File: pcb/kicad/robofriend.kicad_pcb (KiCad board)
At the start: 2 copper layers, 124 parts, among them J1 I2C, J10 BAT2, J11 5VIN, J12 BAT3, J13 3V3OUT, J14 3V3OUT, J15 SPI, J16 MON, J17 M1, J18 M2, J19 US4, J2 ADC1, J20 5VOUT, J21 5VOUT, J22 US3, J23 US2, J24 US1, J25 I2C, J26 I2C, J27 I2C, J28 ADC4, J29 AMP, J3 ADC2, J30 PWR, J31 MLe, J32 USB_A_4_PIN, J4 UART, J5 ADC3, J6 ADC4, J7 BAT1, J8 MRi, J9 12VOUT, K2 SCHRACK-RTx3, Q1 NMOS, Q2 NMOS, Q3 NPN, Q4 PMOS, Q5 NMOS, Q6 NMOS, Q7 NMOS, Q8 NMOS, U1 Teensy++2.0, U2 LM4040, U3 LM321, U4 LM321, U5 LM3940-3.3

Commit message: first steps of layouting done
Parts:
- removed the C14 at (55.9, 120.7)
- removed the C20 at (68.6, 106.0)
- removed the D12 at (64.8, 129.5)
- removed the J29 at (-3.81, 119.4)
- removed K2: SCHRACK-RTx3, SLA_12VDC:Relay_SPST_Schrack-RTx3_RM3.5mm
- removed the Q2 at (88.9, 162.6)
- removed the R19 at (91.1, 143.2)
- removed the R20 at (91.1, 146.4)
- removed the R9 at (92.7, 172.1)
- removed the U4 at (84.1, 147.0)
- added C17: 1n, Capacitors_SMD:C_0805, F.Cu at (206.4, 130.2)
- added C18: 10n, Capacitors_SMD:C_0805, F.Cu at (206.4, 134.0)
- added C21: 100n, Capacitors_SMD:C_0805, F.Cu at (215.3, 137.2)
- added C24: 100n, Capacitors_SMD:C_0805, F.Cu at (219.7, 130.8)
- added C4: 33u, Capacitors_SMD:CP_Elec_4x5.7, F.Cu at (175.3, 59.1)
- added C5: 100u, Capacitors_SMD:CP_Elec_6.3x5.7, F.Cu at (117.5, 65.4)
- added C6: 33u, Capacitors_SMD:CP_Elec_5x5.7, F.Cu at (127.6, 87.0)
- added D15: BAT54, Diodes_SMD:D_SOD-323, F.Cu at (143.8, 124.1)
- added D16: BAT54, Diodes_SMD:D_SOD-323, F.Cu at (143.8, 121.0)
- added D2: D, Diodes_SMD:D_SOD-323, F.Cu at (115.6, 88.9)
- added D20: BAT54, Diodes_SMD:D_SOD-123, F.Cu at (208.3, 141.6)
- added J33: GS2, Connectors:GS2, F.Cu at (219.7, 138.4)
- added J8: GS2, Connectors:GS2, F.Cu at (121.9, 85.7)
- added JP3: JP, Pin_Headers:Pin_Header_Straight_1x02_Pitch2.54mm, F.Cu at (152.1, 121.0)
- added K1: SCHRACK-RTx3, Relay:SPST_Schrack-RTx3_RM3.5mm, F.Cu at (114.3, 69.8)
- added R1: 4.7k, Resistors_SMD:R_0805, F.Cu at (141.0, 91.4)
- added R13: 12k, Resistors_SMD:R_0805, F.Cu at (141.9, 124.1)
- added R18: 39k, Resistors_SMD:R_0805, F.Cu at (140.0, 121.0)
- added R2: 47k, Resistors_SMD:R_0805, F.Cu at (135.9, 91.4)
- added R3: 20k, Resistors_SMD:R_0805, F.Cu at (117.5, 92.1)
- added R4: 10k, Resistors_SMD:R_0805, F.Cu at (120.7, 92.1)
- added R5: 1M, Resistors_SMD:R_0805, F.Cu at (121.9, 88.9)
- added U5: MCP6001, TO_SOT_Packages_SMD:SOT-23-5, F.Cu at (147.0, 122.2)
- added U6: INA193, TO_SOT_Packages_SMD:SOT-23-5, F.Cu at (215.3, 134.0)
- added U7: TL331, TO_SOT_Packages_SMD:SOT-23-5, F.Cu at (219.7, 134.0)
- C10: renamed from C18; moved to B.Cu
- C11: value 15n -> 47u; footprint Capacitors_SMD:C_0805 -> Capacitors_SMD:CP_Elec_6.3x5.8
- C12: value 100n -> 470u; footprint Capacitors_SMD:C_0805 -> Capacitors_SMD:CP_Elec_8x10.5
- C13: renamed from C21; moved to B.Cu
- C14: renamed from C22; moved to B.Cu
- C15: renamed from C3; moved to B.Cu
- C16: renamed from C4; moved to B.Cu
- C19: value 47u -> 1n; footprint Capacitors_SMD:CP_Elec_6.3x5.3 -> Capacitors_SMD:C_0805
- C20: renamed from C5; moved to B.Cu
- C22: renamed from C6; moved to B.Cu
- C26: renamed from C7; moved to B.Cu
- C27: renamed from C8; moved to B.Cu
- C7: renamed from C15; moved to B.Cu
- C8: renamed from C16; moved to B.Cu
- C9: renamed from C17; moved to B.Cu
- D1: renamed from D10; value 10V -> 6V2
- D11: renamed from D8; moved to B.Cu
- D12: renamed from D9; moved to B.Cu
- D13: renamed from D20; moved to B.Cu
- D14: renamed from D21; moved to B.Cu
- D18: renamed from D2; moved to B.Cu
- D19: renamed from D3; moved to B.Cu
- D21: renamed from D6; moved to B.Cu
- D22: renamed from D7; moved to B.Cu
- D23: renamed from D4; moved to B.Cu
- D24: renamed from D5; moved to B.Cu
- J21: renamed from J16; value MON -> MON/AMP
- Q1: footprint TO_SOT_Packages_THT:TO-220-3_Vertical -> TO_SOT_Packages_SMD:SOT-23
- Q2: renamed from Q7; moved to B.Cu
- Q3: renamed from Q8; moved to B.Cu
- R10: renamed from R26; moved to B.Cu
- R11: renamed from R27; moved to B.Cu
- R12: renamed from R5; moved to B.Cu
- R14: renamed from R10; value 100k -> 18k
- R16: renamed from R11; value 27k -> 3k
- R19: renamed from R21; moved to B.Cu
- R23: renamed from R2; moved to B.Cu
- R24: renamed from R17; value 1k -> 100
- R25: renamed from R18; value 1k -> 100
- R26: renamed from R4; moved to B.Cu
- R29: renamed from R3; moved to B.Cu
- R7: renamed from R6; moved to B.Cu
- R8: renamed from R7; moved to B.Cu
- R9: renamed from R8; value 909 -> 910; moved to F.Cu
- U3: value LM321 -> TL331
- U4: renamed from U2; moved to F.Cu
- moved J20 220.2 mm to (201.9, 45.1), turned to 180 degrees
- moved R27 207.3 mm to (203.8, 114.9), turned to 90 degrees
- moved R11 206.0 mm to (191.1, 81.9), turned to 270 degrees
- moved Q6 205.4 mm to (194.9, 113.0), turned to 180 degrees
- moved R28 203.7 mm to (203.8, 117.5), turned to 270 degrees
- moved R30 201.8 mm to (194.9, 115.6)
- moved R10 200.6 mm to (191.1, 79.4), turned to 90 degrees
- moved Q7 199.3 mm to (194.9, 118.1), turned to 180 degrees
- moved Q2 198.6 mm to (188.0, 78.7), turned to 180 degrees
- moved R31 195.4 mm to (194.9, 120.7)
- moved C14 193.5 mm to (199.4, 71.8), turned to 180 degrees
- moved Q3 193.5 mm to (188.0, 82.5), turned to 180 degrees
- moved C13 191.6 mm to (195.6, 71.8), turned to 0 degrees
- moved C23 180.5 mm to (214.0, 115.6)
- moved C25 180.0 mm to (214.0, 119.4)
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- renumbered C13 to C1, C1 to C2, C9 to C23, C10 to C25, C2 to C3, D19 to D10, D13 to D17, D11 to D3, D1 to D4, D14 to D5, D15 to D6, D16 to D7, D17 to D8, D18 to D9, J7 to J1, J22 to J10, J19 to J11, J1 to J12, J25 to J13, J26 to J14, J27 to J15, J9 to J16, J11 to J17, J20 to J18, J21 to J19, J10 to J2, J32 to J20, J6 to J22, J8 to J23, J15 to J24, J28 to J25, J31 to J26, J17 to J27, J18 to J28, J2 to J29, J12 to J3, J3 to J30, J4 to J31, J5 to J32, J30 to J4, J24 to J5, J13 to J6, J14 to J7, J23 to J9, JP6 to JP2, JP3 to JP4, JP4 to JP5, JP2 to JP6, JP5 to JP7, Q3 to Q4, Q4 to Q5, Q5 to Q6, Q6 to Q7, R12 to R15, R13 to R17, R14 to R20, R15 to R21, R16 to R22, R22 to R27, R23 to R28, R24 to R30, R25 to R31, R1 to R6, U5 to U1, U1 to U2
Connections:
- C10 pad 2: +SW -> +12V
- C11 pad 1: Net-(C11-Pad1) -> +12V
- C11 pad 2: +SW -> GND
- C12 pad 1: GND -> +12V
- C12 pad 2: F0 -> GND
- C19 pad 1: +SW -> Net-(C18-Pad2)
- C7 pad 2: +SW -> +12V
- C8 pad 2: +SW -> +12V
- C9 pad 2: +SW -> +12V
- D1 pad 1: Net-(C11-Pad1) -> Net-(D1-Pad1)
- D1 pad 2: Net-(D1-Pad1) -> GND
- D10 pad 1: Net-(D19-Pad1) -> (no net)
- D10 pad 2: Net-(D19-Pad2) -> (no net)
- D3 pad 1: +SW -> -SW
- D3 pad 2: Net-(D11-Pad2) -> Net-(D3-Pad2)
- D4 pad 1: Net-(D1-Pad1) -> GND
- D5 pad 1: Net-(D14-Pad1) -> (no net)
- D5 pad 2: Net-(D14-Pad2) -> (no net)
- D6 pad 1: Net-(D15-Pad1) -> (no net)
- D6 pad 2: Net-(D15-Pad2) -> (no net)
- D7 pad 1: Net-(D16-Pad1) -> (no net)
- D7 pad 2: Net-(D16-Pad2) -> (no net)
- D8 pad 1: Net-(D17-Pad1) -> (no net)
- D8 pad 2: Net-(D17-Pad2) (its old number) -> (no net)
- D9 pad 1: Net-(D18-Pad1) (its old number) -> (no net)
- D9 pad 2: Net-(D18-Pad2) -> (no net)
- J1 pad 1: -SW -> +SW
- J16 pad 1: +SW -> +12V
- J2 pad 1: -SW -> +SW
- J20 pad 2: Net-(J32-Pad2) (its old number) -> (no net)
- J20 pad 3: Net-(J32-Pad3) -> (no net)
- J21 pad 1: Net-(J16-Pad1) -> +12V
- J21 pad 2: Net-(J16-Pad2) -> +12V
- J21 pad 3: Net-(J16-Pad3) -> +5V
- J21 pad 4: Net-(J16-Pad4) -> GND
- J21 pad 5: Net-(J16-Pad5) -> GND
- J21 pad 6: Net-(J16-Pad6) -> GND
- J23 pad 7: Net-(J8-Pad7) -> (no net)
- J23 pad 8: Net-(J8-Pad8) -> (no net)
- J23 pad 9: Net-(J8-Pad9) -> (no net)
- J26 pad 7: Net-(J31-Pad7) -> (no net)
- J26 pad 8: Net-(J31-Pad8) -> (no net)
- J26 pad 9: Net-(J31-Pad9) -> (no net)
- J3 pad 1: -SW -> +SW
- J4 pad 2: +12P -> +SW
- Q1 pad 1: GND -> Net-(D3-Pad2)
- Q1 pad 2: Net-(C11-Pad1) -> Net-(Q1-Pad2)
- Q1 pad 3: Net-(D1-Pad1) -> GND
- Q5 pad 3: +SW -> +12V
- R14 pad 1: F0 -> Net-(D15-Pad2)
- R14 pad 2: +SW -> +12V
- R16 pad 1: F0 -> Net-(D15-Pad2)
- R20 pad 1: +SW -> +12V
- R24 pad 1: Net-(R17-Pad1) -> Net-(C17-Pad2)
- R25 pad 1: Net-(R18-Pad1) -> Net-(C18-Pad2)
- R6 pad 1: +SW -> +12V
- R9 pad 2: AREF -> Net-(JP3-Pad2)
- RV1 pad 1: +SW -> Net-(D1-Pad1)
- RV1 pad 2: Net-(Q2-Pad2) -> Net-(RV1-Pad2)
- RV1 pad 3: Net-(D1-Pad1) -> Net-(R2-Pad1)
- U2 pad 24: /F7 -> (no net)
- U2 pad 25: /F6 -> F6
- U2 pad 43: Net-(U1-Pad43) -> (no net)
- U2 pad 44: Net-(U1-Pad44) -> (no net)
- U2 pad 45: Net-(U1-Pad45) -> (no net)
- U2 pad 46: Net-(U1-Pad46) -> (no net)
- U2 pad 47: Net-(U1-Pad47) -> (no net)
- U2 pad 48: Net-(U1-Pad48) -> (no net)
- U2 pad 49: Net-(U1-Pad49) -> (no net)
- U2 pad 50: Net-(U1-Pad50) -> (no net)
- U2 pad 51: Net-(U1-Pad51) -> (no net)
- U2 pad 52: Net-(U1-Pad52) -> (no net)
- U3 pad 1: Net-(R17-Pad1) -> Net-(RV1-Pad2)
- U3 pad 3: Net-(R18-Pad1) -> Net-(J8-Pad2)
- U3 pad 4: Net-(R20-Pad1) -> Net-(Q1-Pad2)
- U3 pad 5: +5V -> Net-(D2-Pad1)
- U4 pad 1: AREF -> Net-(JP3-Pad2)
- U4 pad 3: Net-(U2-Pad3) -> (no net)
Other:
- net class Power added: clearance 0.2, trace_width 1, via_dia 0.6, via_drill 0.4
- board text added: "1"
- board text added: "12V"
- board text added: "2"
- board text added: "3"
- board text added: "3V3"
- board text added: "4"
- board text added: "5V"
- board text added: "ADC1"
- board text added: "ADC2"
- board text added: "BAT1"
- board text added: "Boost"
- board text added: "Buck-In"
- board text added: "Buck-Out"
- board text added: "ECHO"
- board text added: "GND"
- board text added: "I2C"
- board text added: "IR1"
- board text added: "IR2"
- board text added: "IR3"
- board text added: "MISO"
- board text added: "MLe"
- board text added: "MOSI"
- board text added: "MRi"
- board text added: "Main-Switch"
- board text added: "Monitor/Amp"
- board text added: "RST"
- board text added: "RX"
- board text added: "RoboFriend - Power PCB Designed by Martin Zahedi University of Applied Sciences - Technikum Wien"
- board text added: "SCK"
- board text added: "SCL"
- board text added: "SDA"
- board text added: "SIG"
- board text added: "SPI"
- board text added: "SS"
- board text added: "TRIG"
- board text added: "TX"
- board text added: "UART"
- board text added: "Ultrasonic"
- board text added: "VCC"

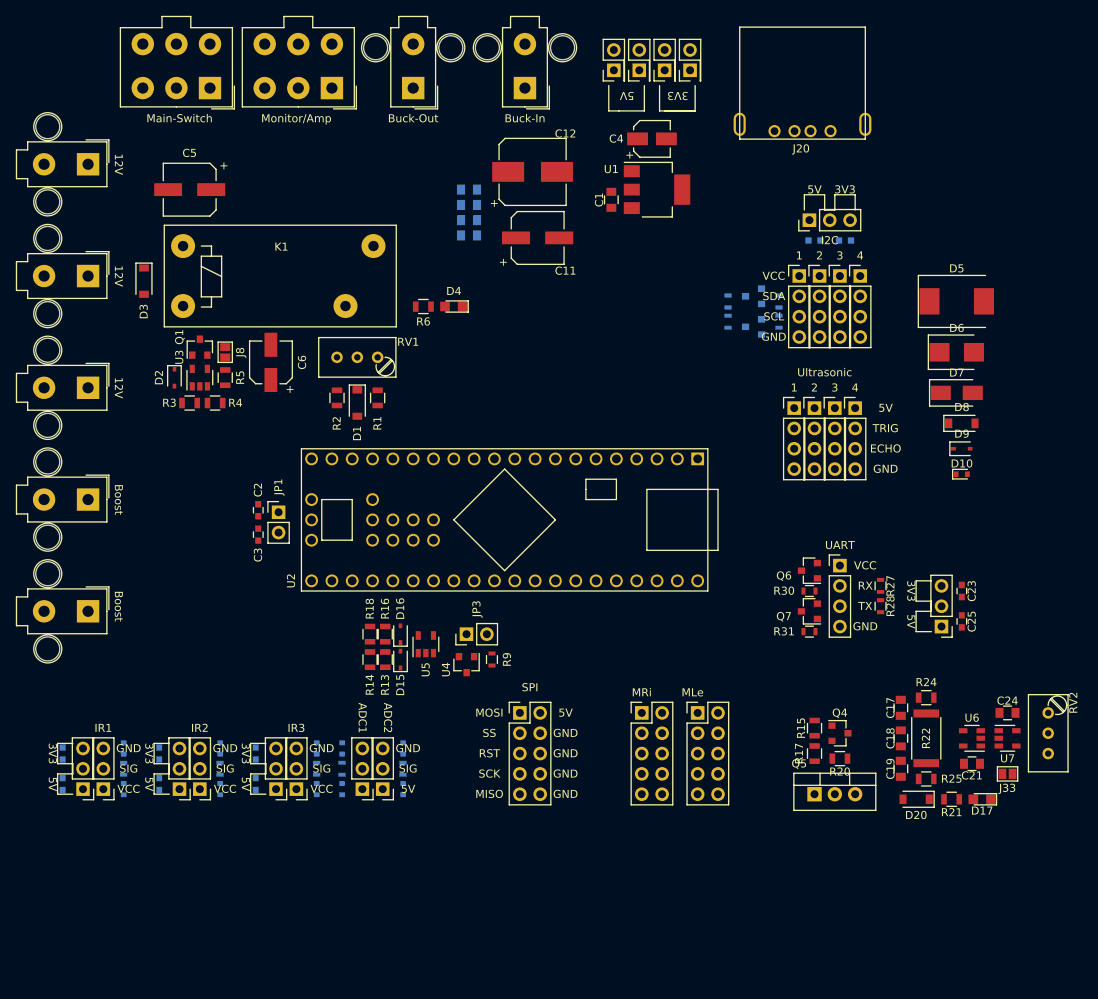
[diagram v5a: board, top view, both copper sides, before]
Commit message: adopted pin headers in layout
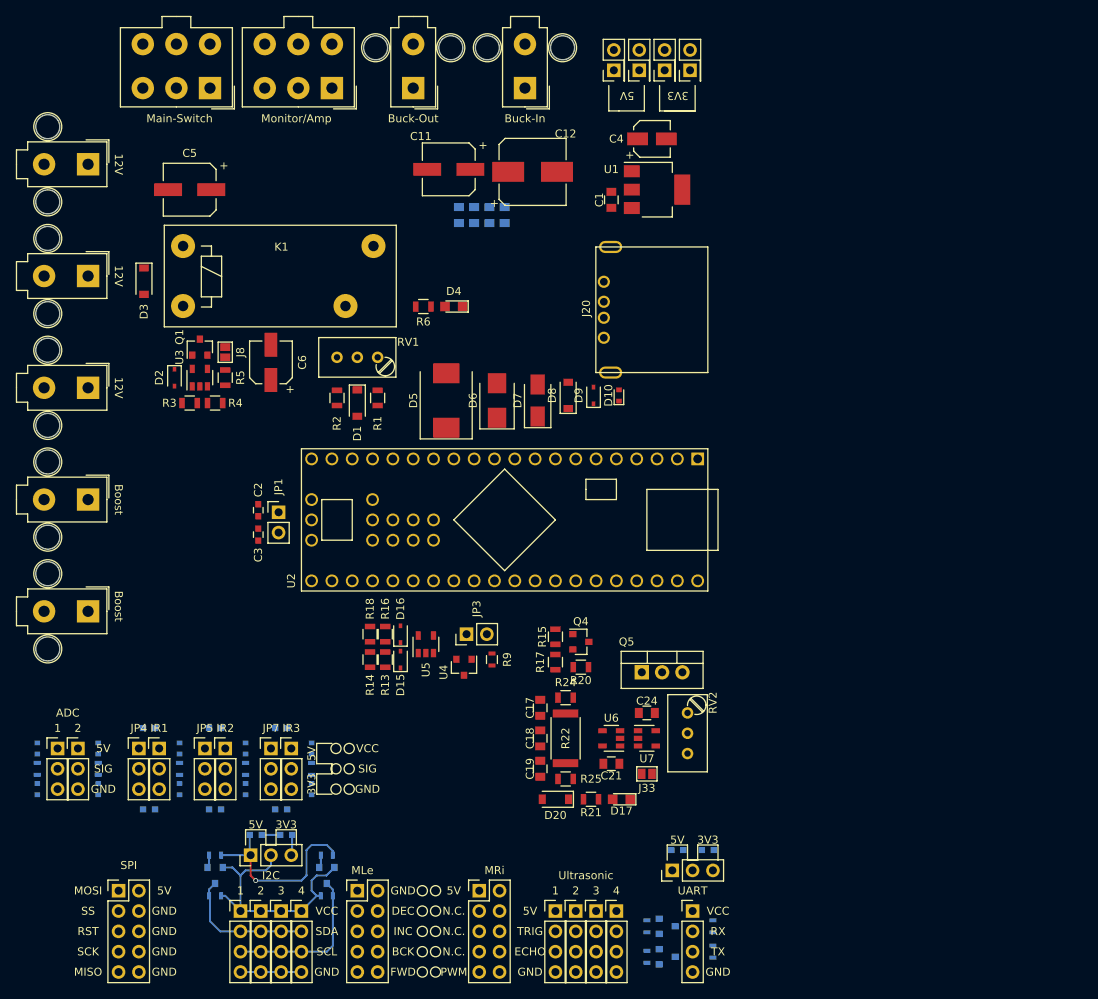
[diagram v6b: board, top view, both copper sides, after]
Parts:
- C23, C25, Q6, Q7, R27, R28, R30, R31: moved to B.Cu
- moved J12 105.7 mm to (123.8, 155.6)
- moved J13 105.7 mm to (126.4, 155.6)
- moved J14 105.7 mm to (128.9, 155.6)
- moved J15 105.7 mm to (131.4, 155.6)
- moved JP2 105.7 mm to (125.1, 148.6)
- moved C13 102.0 mm to (125.7, 146.1)
- moved C14 102.0 mm to (129.5, 146.1)
- moved Q2 98.8 mm to (120.7, 151.1), turned to 270 degrees
- moved R10 98.8 mm to (120.7, 148.6), turned to 180 degrees
- moved R7 98.1 mm to (120.7, 153.7), turned to 180 degrees
- moved R8 87.6 mm to (134.6, 153.7), turned to 0 degrees
- moved R11 87.4 mm to (134.6, 148.6), turned to 180 degrees
- moved Q3 86.9 mm to (134.6, 151.1), turned to 270 degrees
- moved J10 69.6 mm to (168.3, 155.6)
- moved J11 69.6 mm to (170.8, 155.6)
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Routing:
- net Net-(J12-Pad1): track 0.00 -> 32.4 mm
- net +5V: track 0.00 -> 23.7 mm, vias 0 -> 1
- net Net-(J12-Pad3): track 0.00 -> 19.9 mm
- net Net-(J12-Pad2): track 0.00 -> 17.1 mm
- net GND: track 0.00 -> 9.93 mm
- net +3V3: track 0.00 -> 2.59 mm
- net D0: track 0.00 -> 1.62 mm
- net D1: track 0.00 -> 1.62 mm
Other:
- net class 10A added: clearance 0.2, trace_width 2.5, via_dia 0.6, via_drill 0.4
- net class 3A added: clearance 0.2, trace_width 0.48, via_dia 0.6, via_drill 0.4
- net class 5A added: clearance 0.2, trace_width 0.96, via_dia 0.6, via_drill 0.4
- net class Power removed
- board text added: "ADC"
- board text added: "BCK"
- board text added: "DEC"
- board text added: "FWD"
- board text added: "INC"
- board text added: "N.C."
- board text added: "PWM"
- board text removed: "ADC1"
- board text removed: "ADC2"

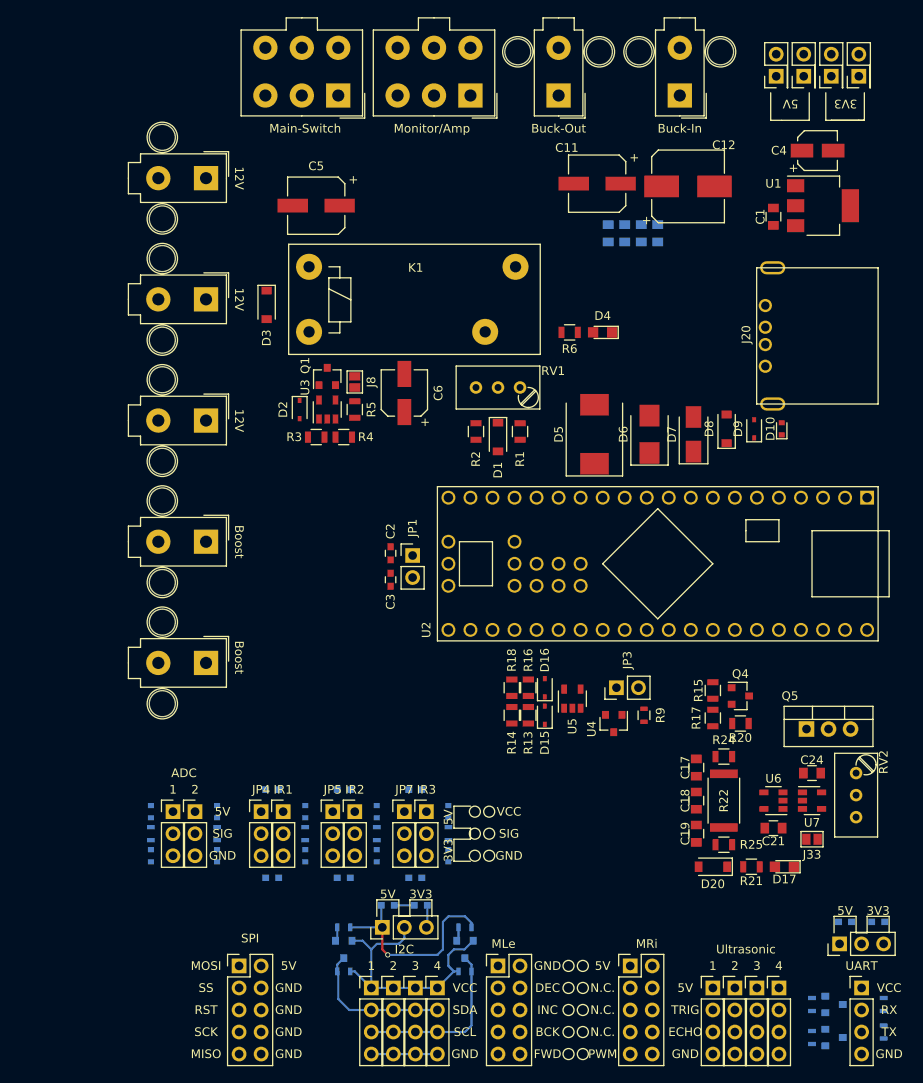
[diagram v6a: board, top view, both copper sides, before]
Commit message: added plugs for buck-boost converter module
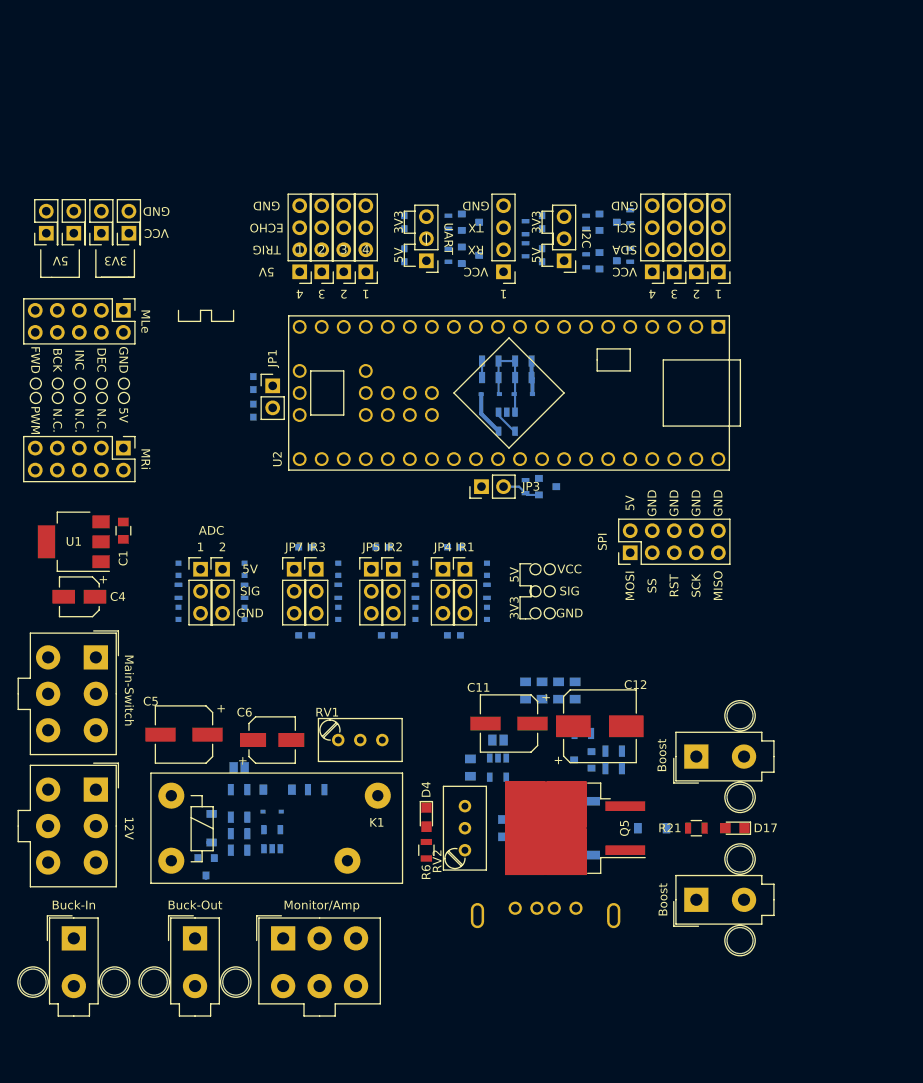
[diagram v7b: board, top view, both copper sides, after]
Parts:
- removed D10: D, Diodes_SMD:D_SOD-523
- removed D5: D, Diodes_SMD:D_SMC
- removed D6: D, Diodes_SMD:D_SMB
- removed D7: D, Diodes_SMD:D_SMA
- removed D8: D, Diodes_SMD:D_SOD-123
- removed D9: D, Diodes_SMD:D_SOD-323
- removed J2: BAT2, Connectors_Molex:Molex_MiniFit-JR-5556-02B_2x01x4.20mm_Straight
- removed J3: BAT3, Connectors_Molex:Molex_MiniFit-JR-5556-02B_2x01x4.20mm_Straight
- C17, C18, C19, C2, C21, C24, C3, D1, D15, D16, D2, D3, J20, J33, J8, Q1, Q4, R1, R13, R14, R15, R16, R17, R18, R2, R20, R22, R24, R25, R3, R4, R5, R9, U3, U4, U5, U6, U7: moved to B.Cu
- D20: value BAT54 -> DB2X41500L; moved to B.Cu
- J1: value BAT1 -> PWR; footprint Connectors_Molex:Molex_MiniFit-JR-5556-02B_2x01x4.20mm_Straight -> Connectors_Molex:Molex_MiniFit-JR-5556-06A_2x03x4.20mm_Straight
- J22: value ADC4 -> ADC1
- J25: value ADC4 -> ADC2
- J29: value ADC1 -> IR1
- J30: value ADC2 -> IR2
- J32: value ADC3 -> IR3
- Q5: footprint TO_SOT_Packages_THT:TO-220-3_Vertical -> TO_SOT_Packages_SMD:TO-263-2
- moved J17 119.7 mm to (89.5, 149.9), turned to 0 degrees
- moved J16 105.8 mm to (103.5, 149.9), turned to 0 degrees
- moved Q7 102.9 mm to (135.3, 67.3)
- moved R31 102.9 mm to (132.7, 67.3)
- moved R28 101.5 mm to (141.6, 67.9), turned to 90 degrees
- moved J21 99.5 mm to (113.7, 149.9), turned to 0 degrees
- moved C4 99.4 mm to (90.2, 110.5), turned to 180 degrees
- moved J11 99.3 mm to (115.6, 73.0), turned to 180 degrees
- moved C25 97.4 mm to (127.6, 67.3), turned to 270 degrees
- moved J10 96.6 mm to (118.1, 73.0), turned to 180 degrees
- moved R27 96.3 mm to (141.6, 70.5), turned to 90 degrees
- moved Q6 96.0 mm to (135.3, 71.1)
- moved R30 96.0 mm to (132.7, 71.1)
- moved U1 94.6 mm to (89.5, 104.1), turned to 180 degrees
- moved J9 94.1 mm to (120.7, 73.0), turned to 180 degrees
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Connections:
- J1 pad 2: GND -> +SW
- J4 pad 3: GND -> -SW
- J4 pad 6: -SW -> GND
- K1 pad 14: -SW -> +SW
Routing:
- net Net-(J12-Pad1): track 32.4 -> 0.00 mm
- net Net-(J12-Pad3): track 19.9 -> 0.00 mm
- net +5V: track 23.7 -> 5.41 mm, vias 1 -> 0
- net Net-(J12-Pad2): track 17.1 -> 0.00 mm
- net Net-(D15-Pad2): track 0.00 -> 11.7 mm
- net GND: track 9.93 -> 4.44 mm
- net Net-(JP3-Pad2): track 0.00 -> 4.47 mm
- net F0: track 0.00 -> 3.05 mm
- net +3V3: track 2.59 -> 0.16 mm
- net +12V: track 0.00 -> 1.91 mm
- net D0: track 1.62 -> 0.00 mm
- net D1: track 1.62 -> 0.00 mm
- net Net-(C6-Pad1): track 0.00 -> 1.61 mm
- net Net-(D3-Pad2): track 0.00 -> 0.81 mm
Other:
- net class 10A: trace_width 2.5 -> 2
- board text removed: "Ultrasonic"

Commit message: layout almost done. the decision about the level shifters needs to be made
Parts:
- removed the C13 at (143.5, 71.1)
- removed the C14 at (143.5, 67.3)
- removed the C15 at (133.3, 104.8)
- removed the C16 at (133.3, 114.9)
- removed C20, C22, C23, C25, C26, C27: 100n, Capacitors_SMD:C_0603
- removed the JP4 at (132.1, 107.3)
- removed JP7: Jumper, Pin_Headers:Pin_Header_Straight_1x03_Pitch2.54mm
- added C18: 100n, Capacitors_SMD:C_0603, F.Cu at (108.6, 97.2)
- added C19: 100n, Capacitors_SMD:C_0603, F.Cu at (108.6, 98.4)
- added J12: 12V-Buck-Boost, Connectors_Molex:Molex_MiniFit-JR-5556-02B_2x01x4.20mm_Straight, F.Cu at (132.7, 149.9)
- added J20: 12V-Reg, Connectors_Molex:Molex_MiniFit-JR-5556-02B_2x01x4.20mm_Straight, F.Cu at (146.7, 149.9)
- added J34: UART, Pin_Headers:Pin_Header_Straight_1x04_Pitch2.54mm, F.Cu at (102.2, 90.2)
- added U8: TXS0102, Housings_SSOP:SSOP-8_2.95x2.8mm_Pitch0.65mm, F.Cu at (108.6, 93.3)
- J11: renamed from J16; value 12VOUT -> 12V-Buck
- moved J18 104.1 mm to (99.7, 69.2), turned to 0 degrees
- moved D5 24.2 mm to (125.7, 109.2)
- moved D6 24.2 mm to (125.7, 114.3)
- moved JP4 24.2 mm to (148.0, 109.2)
- moved R12 24.2 mm to (125.7, 111.8)
- moved J22 19.1 mm to (123.2, 109.2)
- moved J25 14.1 mm to (120.7, 109.2)
- moved J32 12.8 mm to (130.2, 109.2)
- moved D17 12.8 mm to (132.7, 109.2)
- moved D18 12.8 mm to (132.7, 114.3)
- moved R29 12.8 mm to (132.7, 111.8)
- moved C1 12.5 mm to (106.7, 108.0)
- moved U1 12.5 mm to (101.0, 109.2)
- moved C4 12.5 mm to (101.6, 115.6)
- moved D7 9.09 mm to (118.1, 109.2)
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- renumbered C17 to C13, C18 to C14, C19 to C15, C21 to C16, C24 to C17, D16 to D10, D17 to D11, D18 to D12, D19 to D13, D20 to D14, D21 to D15, D22 to D16, D23 to D17, D24 to D18, D11 to D5, D12 to D6, D13 to D7, D14 to D8, D15 to D9, J5 to J10, J17 to J13, J18 to J14, J19 to J15, J9 to J16, J10 to J17, J20 to J18, J11 to J19, J4 to J2, J6 to J3, J7 to J4, J8 to J5, J12 to J6, J13 to J7, J14 to J8, J15 to J9, JP5 to JP4, JP6 to JP5
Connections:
- D12 pad 1: Net-(D18-Pad1) -> Net-(D12-Pad1)
- D15 pad 1: Net-(D21-Pad1) -> Net-(D12-Pad1)
- D17 pad 1: Net-(D23-Pad1) -> Net-(D12-Pad1)
- J21 pad 1: +12V -> Net-(J20-Pad1)
- J21 pad 2: +12V -> Net-(J20-Pad1)
- J29 pad 1: Net-(D18-Pad1) -> Net-(D12-Pad1)
- J30 pad 1: Net-(D21-Pad1) -> Net-(D12-Pad1)
- J32 pad 1: Net-(D23-Pad1) -> Net-(D12-Pad1)
- JP4 pad 2: Net-(D21-Pad1) -> Net-(D12-Pad1)
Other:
- board text added: "12V-BAT"
- board text added: "Buck-Boost-In"
- board text added: "Buck-Boost-Out"
- board text added: "IR"
- board text removed: "12V"
- board text removed: "IR1"
- board text removed: "IR2"
- board text removed: "IR3"
